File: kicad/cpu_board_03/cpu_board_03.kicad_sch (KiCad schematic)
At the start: 53 parts, among them J1 DIN41612_02x32_AC, J10 PLD_aux, J11 Conn_01x09, J6 Conn_01x02_Socket, J7 Jmp_Irq, J8 Jmp_NMI, J9 Ram1 Enable, SW1 SW_Reset, SW2 SW_PWR, U1 W65C02SxP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

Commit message: routing cpu 3 board
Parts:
- removed J7: Jmp_Irq, Connector_PinHeader_2.54mm:PinHeader_1x02_P2.54mm_Vertical, symbol Connector:Conn_01x02_Pin
- removed J8: Jmp_NMI, Connector_PinHeader_2.54mm:PinHeader_1x02_P2.54mm_Vertical, symbol Connector:Conn_01x02_Pin
- added C1: 47uF, Capacitor_THT:CP_Radial_D4.0mm_P2.00mm, symbol Device:C_Polarized
- added R3, R5: 10K, Resistor_SMD:R_0805_2012Metric_Pad1.20x1.40mm_HandSolder, symbol Device:R
- C3: footprint Package_SO:SO-20_12.8x7.5mm_P1.27mm -> Capacitor_SMD:C_0805_2012Metric_Pad1.18x1.45mm_HandSolder
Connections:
- net AB0: now also J1.a18 (Pin_a18); no longer J1.a17 (Pin_a17)
- net AB1: now also J1.c18 (Pin_c18); no longer J1.a16 (Pin_a16)
- net AB10: now also J1.a13 (Pin_a13); no longer J1.a7 (Pin_a7)
- net AB11: now also J1.c13 (Pin_c13); no longer J1.a6 (Pin_a6)
- net AB12: now also J1.a12 (Pin_a12); no longer J1.a5 (Pin_a5)
- net AB13: now also J1.c12 (Pin_c12); no longer J1.a4 (Pin_a4)
- net AB14: now also J1.a11 (Pin_a11); no longer J1.a3 (Pin_a3)
- net AB15: now also J1.c11 (Pin_c11); no longer J1.a2 (Pin_a2)
- net AB2: now also J1.a17 (Pin_a17); no longer J1.a15 (Pin_a15)
- net AB3: now also J1.c17 (Pin_c17); no longer J1.a14 (Pin_a14)
- net AB4: now also J1.a16 (Pin_a16); no longer J1.a13 (Pin_a13)
- net AB5: now also J1.c16 (Pin_c16); no longer J1.a12 (Pin_a12)
- net AB6: now also J1.a15 (Pin_a15); no longer J1.a11 (Pin_a11)
- net AB7: now also J1.c15 (Pin_c15); no longer J1.a10 (Pin_a10)
- net AB8: now also J1.a14 (Pin_a14); no longer J1.a9 (Pin_a9)
- net AB9: now also J1.c14 (Pin_c14); no longer J1.a8 (Pin_a8)
- net CLOCK: no longer U9.7 (~{ST})
- net DB0: now also J1.a5 (Pin_a5); no longer J1.c9 (Pin_c9)
- net DB1: now also J1.c5 (Pin_c5); no longer J1.c8 (Pin_c8)
- net DB2: now also J1.a4 (Pin_a4); no longer J1.c7 (Pin_c7)
- net DB3: now also J1.c4 (Pin_c4); no longer J1.c6 (Pin_c6)
- net DB4: now also J1.a3 (Pin_a3); no longer J1.c5 (Pin_c5)
- net DB5: now also J1.c3 (Pin_c3); no longer J1.c4 (Pin_c4)
- net DB6: now also J1.a2 (Pin_a2); no longer J1.c3 (Pin_c3)
- net GND: now also J1.c10 (Pin_c10), J1.c27 (Pin_c27), J1.c6 (Pin_c6), C1.2; no longer J1.c18 (Pin_c18)
- net PLD_O0: now also J1.c9 (Pin_c9)
- net PLD_O7: now also J1.c8 (Pin_c8)
- net SYS_CLK: now also J1.a7 (Pin_a7), U9.7 (~{ST}); no longer J1.a22 (Pin_a22)
- net VCC: now also J1.a10 (Pin_a10), J1.a27 (Pin_a27), J1.a6 (Pin_a6), C1.1, R3.1, R5.1; no longer J1.a18 (Pin_a18)
- net ~{IOEN_00_GPIO0}: now also J1.a26 (Pin_a26); no longer J1.a31 (Pin_a31)
- net ~{IOEN_01}: now also J1.c26 (Pin_c26); no longer J1.a30 (Pin_a30)
- net ~{IOEN_02_UART}: now also J1.a25 (Pin_a25)
- net ~{IOEN_03}: now also J1.c25 (Pin_c25); no longer J1.a28 (Pin_a28)
- net ~{IOEN_04}: now also J1.a24 (Pin_a24); no longer J1.a27 (Pin_a27)
- net ~{IOEN_05}: now also J1.c24 (Pin_c24); no longer J1.a26 (Pin_a26)
- net ~{IOEN_06}: now also J1.a23 (Pin_a23); no longer J1.a25 (Pin_a25)
- net ~{IOEN_07}: now also J1.c23 (Pin_c23); no longer J1.a24 (Pin_a24)
- net ~{IO_SEL}: now also J1.a8 (Pin_a8); no longer J1.a23 (Pin_a23)
- net ~{IRQ}: now also J1.a31 (Pin_a31), R5.2
- net ~{NMI}: now also J1.a30 (Pin_a30), R3.2
- net ~{SYS_CLK}: now also J1.c7 (Pin_c7); no longer J1.a21 (Pin_a21)
- net ~{IOEN_02}: no longer names the net of J1.a29 (Pin_a29)
- no-connect marks 30 -> 12

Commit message: more routing on cpu board v3
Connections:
- net ~{CS_RAM0}: now also U4.20 (O3); no longer U4.19 (O4)
- net ~{CS_RAM1}: now also U4.19 (O4); no longer U4.20 (O3)
- net at D8.1 (K): now also RN2.2 (R2.1); no longer RN2.4 (R4.1)
- net at D3.1 (K): now also RN1.1 (R1.1); no longer RN1.3 (R3.1)
- net at D9.2 (A): now also RN3.2 (R2.1); no longer RN3.4 (R4.1)
- net at D6.1 (K): now also RN2.4 (R4.1); no longer RN2.2 (R2.1)
- net at D11.2 (A): now also RN3.3 (R3.1); no longer RN3.2 (R2.1)
- net at D10.2 (A): now also RN3.4 (R4.1); no longer RN3.3 (R3.1)
- net at D1.1 (K): now also RN1.3 (R3.1); no longer RN1.1 (R1.1)
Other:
- moved on the sheet: RN1, RN2

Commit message: more routing
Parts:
- added C13, C15, C2: 100nF, Capacitor_SMD:C_0805_2012Metric_Pad1.18x1.45mm_HandSolder, symbol Device:C
- added U12: 74LS138, Package_SO:SO-16_3.9x9.9mm_P1.27mm, symbol 74xx:74LS138
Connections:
- net A4: now also U12.1 (A0)
- net A5: now also U12.2 (A1)
- net A6: now also U12.3 (A2)
- net A7: now also U12.6 (E3)
- net GND: now also J1.c19 (Pin_c19), J1.c29 (Pin_c29), J10.1 (Pin_1), J9.1 (Pin_1), U8.19 (CE), C13.2, C15.2, C2.2, U12.5 (E2), U12.8 (GND); no longer J1.c27 (Pin_c27), J9.3 (Pin_3), U10.1 (A->B), U11.1 (A->B)
- net PLD_I1: now also J10.2 (Pin_2); no longer J10.1 (Pin_1)
- net PLD_O0: no longer J10.2 (Pin_2)
- net RES: now also J1.c31 (Pin_c31); no longer J1.c30 (Pin_c30)
- net VCC: now also J1.a19 (Pin_a19), J1.a29 (Pin_a29), J10.3 (Pin_3), J9.3 (Pin_3), U10.1 (A->B), U11.1 (A->B), C13.1, C15.1, C2.1, U12.16 (VCC); no longer J1.a27 (Pin_a27), J9.1 (Pin_1)
- net ~{IOEN_00_GPIO0}: now also J1.a24 (Pin_a24); no longer J1.a26 (Pin_a26)
- net ~{IOEN_01}: now also J1.c24 (Pin_c24); no longer J1.c26 (Pin_c26)
- net ~{IOEN_02_UART}: now also J1.a23 (Pin_a23); no longer J1.a25 (Pin_a25)
- net ~{IOEN_03}: now also J1.c23 (Pin_c23); no longer J1.c25 (Pin_c25)
- net ~{IOEN_04}: now also J1.a22 (Pin_a22); no longer J1.a24 (Pin_a24)
- net ~{IOEN_05}: now also J1.c22 (Pin_c22); no longer J1.c24 (Pin_c24)
- net ~{IOEN_06}: now also J1.a21 (Pin_a21); no longer J1.a23 (Pin_a23)
- net ~{IOEN_07}: now also J1.c21 (Pin_c21); no longer J1.c23 (Pin_c23)
- net ~{IO_SEL}: now also U12.4 (E1)
- net ~{IRQ}: now also J1.a30 (Pin_a30); no longer J1.a31 (Pin_a31)
- net ~{NMI}: now also J1.c30 (Pin_c30); no longer J1.a30 (Pin_a30)
- net ~{RES}: now also J1.a31 (Pin_a31); no longer J1.c31 (Pin_c31)
- net ~{IO_RD_DIR}: now reaches U8.1 (A->B)
- net ~{IO_RD_DIR}: now also J1.c8 (Pin_c8), U4.16 (O7)
- net ~{IOEN_08}: now reaches J1.a28 (Pin_a28)
- net ~{IOEN_08}: now also U12.15 (O0)
- net ~{IOEN_09}: now reaches J1.c28 (Pin_c28)
- net ~{IOEN_09}: now also U12.14 (O1)
- removed net PLD_O7: J1.c8 (Pin_c8), J10.3 (Pin_3), U4.16 (O7)
- new net ~{IOEN_10}: J1.a27 (Pin_a27), U12.13 (O2)
- new net ~{IOEN_11}: J1.c27 (Pin_c27), U12.12 (O3)
- new net ~{IOEN_12}: J1.a26 (Pin_a26), U12.11 (O4)
- new net ~{IOEN_13}: J1.c26 (Pin_c26), U12.10 (O5)
- new net ~{IOEN_14}: J1.a25 (Pin_a25), U12.9 (O6)
- new net ~{IOEN_15}: J1.c25 (Pin_c25), U12.7 (O7)
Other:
- moved on the sheet: C1, C11, C12, D1, D11, D12, J10, J11, RN1, RN2, RN3, U6

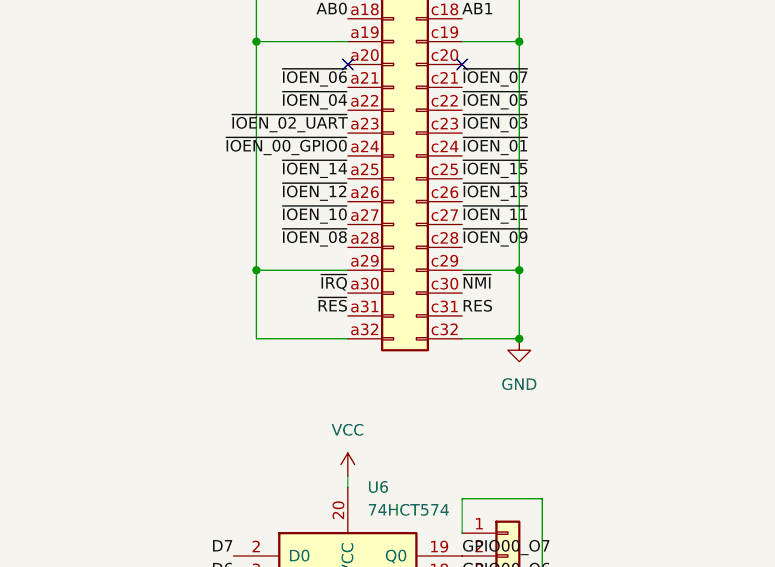
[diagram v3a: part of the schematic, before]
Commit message: shrink board
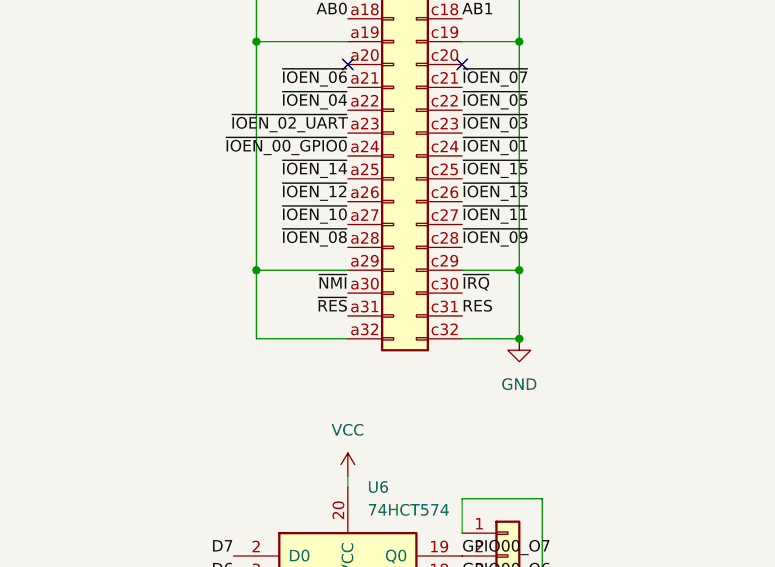
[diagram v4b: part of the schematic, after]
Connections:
- net ~{IRQ}: now also J1.c30 (Pin_c30); no longer J1.a30 (Pin_a30)
- net ~{NMI}: now also J1.a30 (Pin_a30); no longer J1.c30 (Pin_c30)
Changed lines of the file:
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@@
+    (effects (font (size 1.27 1.27)) (justify right bottom))
+  )
+  (label "~{NMI}" (at 351.79 185.42 180) (fields_autoplaced)
     (effects (font (size 1.27 1.27)) (justify right bottom))
   )
@@
     (effects (font (size 1.27 1.27)) (justify left bottom))
   )
-  (label "~{IRQ}" (at 351.79 185.42 180) (fields_autoplaced)
-    (effects (font (size 1.27 1.27)) (justify right bottom))
-  )
   (label "A3" (at 261.62 175.26 0) (fields_autoplaced)
     (effects (font (size 1.27 1.27)) (justify left bottom))
@@
     (effects (font (size 1.27 1.27)) (justify right bottom))
   )
-  (label "~{NMI}" (at 364.49 185.42 0) (fields_autoplaced)
-    (effects (font (size 1.27 1.27)) (justify left bottom))
-  )
   (label "A1" (at 82.55 135.89 180) (fields_autoplaced)
     (effects (font (size 1.27 1.27)) (justify right bottom))
@@
     (effects (font (size 1.27 1.27)) (justify right bottom))
   )
+  (label "~{IRQ}" (at 364.49 185.42 0) (fields_autoplaced)
+    (effects (font (size 1.27 1.27)) (justify left bottom))
+  )
   (label "D0" (at 339.09 232.41 180) (fields_autoplaced)

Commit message: DRCs pass...
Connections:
- net ~{IOEN_00_GPIO0}: now also J1.a28 (Pin_a28); no longer J1.a24 (Pin_a24)
- net ~{IOEN_01}: now also J1.c28 (Pin_c28); no longer J1.c24 (Pin_c24)
- net ~{IOEN_02_UART}: now also J1.a27 (Pin_a27); no longer J1.a23 (Pin_a23)
- net ~{IOEN_03}: now also J1.c27 (Pin_c27); no longer J1.c23 (Pin_c23)
- net ~{IOEN_04}: now also J1.a26 (Pin_a26); no longer J1.a22 (Pin_a22)
- net ~{IOEN_05}: now also J1.c26 (Pin_c26); no longer J1.c22 (Pin_c22)
- net ~{IOEN_06}: now also J1.a25 (Pin_a25); no longer J1.a21 (Pin_a21)
- net ~{IOEN_07}: now also J1.c25 (Pin_c25); no longer J1.c21 (Pin_c21)
- net ~{IOEN_08}: now also J1.a24 (Pin_a24); no longer J1.a28 (Pin_a28)
- net ~{IOEN_09}: now also J1.c24 (Pin_c24); no longer J1.c28 (Pin_c28)
- net ~{IOEN_10}: now also J1.a23 (Pin_a23); no longer J1.a27 (Pin_a27)
- net ~{IOEN_11}: now also J1.c23 (Pin_c23); no longer J1.c27 (Pin_c27)
- net ~{IOEN_12}: now also J1.a22 (Pin_a22); no longer J1.a26 (Pin_a26)
- net ~{IOEN_13}: now also J1.c22 (Pin_c22); no longer J1.c26 (Pin_c26)
- net ~{IOEN_14}: now also J1.a21 (Pin_a21); no longer J1.a25 (Pin_a25)
- net ~{IOEN_15}: now also J1.c21 (Pin_c21); no longer J1.c25 (Pin_c25)
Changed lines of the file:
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@@
+    (effects (font (size 1.27 1.27)) (justify left bottom))
+  )
+  (label "~{IOEN_10}" (at 351.79 167.64 180) (fields_autoplaced)
+    (effects (font (size 1.27 1.27)) (justify right bottom))
+  )
+  (label "~{IOEN_13}" (at 364.49 165.1 0) (fields_autoplaced)
     (effects (font (size 1.27 1.27)) (justify left bottom))
   )
@@
     (effects (font (size 1.27 1.27)) (justify left bottom))
   )
-  (label "~{IOEN_15}" (at 364.49 172.72 0) (fields_autoplaced)
-    (effects (font (size 1.27 1.27)) (justify left bottom))
+  (label "~{IOEN_14}" (at 351.79 162.56 180) (fields_autoplaced)
+    (effects (font (size 1.27 1.27)) (justify right bottom))
   )
   (label "~{IOEN_12}" (at 175.26 255.27 0) (fields_autoplaced)
@@
     (effects (font (size 1.27 1.27)) (justify right bottom))
   )
+  (label "~{IOEN_06}" (at 351.79 172.72 180) (fields_autoplaced)
+    (effects (font (size 1.27 1.27)) (justify right bottom))
+  )
   (label "DB6" (at 285.75 129.54 0) (fields_autoplaced)
     (effects (font (size 1.27 1.27)) (justify left bottom))
@@
     (effects (font (size 1.27 1.27)) (justify left bottom))
   )
+  (label "~{IOEN_04}" (at 351.79 175.26 180) (fields_autoplaced)
+    (effects (font (size 1.27 1.27)) (justify right bottom))
+  )
   (label "A10" (at 35.56 246.38 180) (fields_autoplaced)
     (effects (font (size 1.27 1.27)) (justify right bottom))
@@
     (effects (font (size 1.27 1.27)) (justify right bottom))
   )
-  (label "~{IOEN_13}" (at 364.49 175.26 0) (fields_autoplaced)
-    (effects (font (size 1.27 1.27)) (justify left bottom))
-  )
   (label "GPIO00_O7" (at 364.49 214.63 0) (fields_autoplaced)
     (effects (font (size 1.27 1.27)) (justify left bottom))
@@
     (effects (font (size 1.27 1.27)) (justify left bottom))
   )
+  (label "~{IOEN_08}" (at 351.79 170.18 180) (fields_autoplaced)
+    (effects (font (size 1.27 1.27)) (justify right bottom))
+  )
   (label "~{IO_RD_DIR}" (at 259.08 137.16 180) (fields_autoplaced)
     (effects (font (size 1.27 1.27)) (justify right bottom))
@@
     (effects (font (size 1.27 1.27)) (justify left bottom))
   )
-  (label "~{IOEN_09}" (at 364.49 180.34 0) (fields_autoplaced)
-    (effects (font (size 1.27 1.27)) (justify left bottom))
-  )
   (label "A0" (at 134.62 135.89 180) (fields_autoplaced)
     (effects (font (size 1.27 1.27)) (justify right bottom))
@@
     (effects (font (size 1.27 1.27)) (justify right bottom))
   )
+  (label "~{IOEN_01}" (at 364.49 180.34 0) (fields_autoplaced)
+    (effects (font (size 1.27 1.27)) (justify left bottom))
+  )
   (label "A1" (at 58.42 119.38 0) (fields_autoplaced)
     (effects (font (size 1.27 1.27)) (justify left bottom))
@@
     (effects (font (size 1.27 1.27)) (justify left bottom))
   )
+  (label "~{IOEN_03}" (at 364.49 177.8 0) (fields_autoplaced)
+    (effects (font (size 1.27 1.27)) (justify left bottom))
+  )
   (label "A3" (at 134.62 143.51 180) (fields_autoplaced)
     (effects (font (size 1.27 1.27)) (justify right bottom))
@@
     (effects (font (size 1.27 1.27)) (justify left bottom))
   )
-  (label "~{IOEN_14}" (at 351.79 172.72 180) (fields_autoplaced)
-    (effects (font (size 1.27 1.27)) (justify right bottom))
-  )
   (label "SYS_CLK" (at 35.56 121.92 180) (fields_autoplaced)
     (effects (font (size 1.27 1.27)) (justify right bottom))
@@
     (effects (font (size 1.27 1.27)) (justify left bottom))
   )
+  (label "~{IOEN_11}" (at 364.49 167.64 0) (fields_autoplaced)
+    (effects (font (size 1.27 1.27)) (justify left bottom))
+  )
   (label "A3" (at 58.42 124.46 0) (fields_autoplaced)
     (effects (font (size 1.27 1.27)) (justify left bottom))
@@
     (effects (font (size 1.27 1.27)) (justify right bottom))
   )
+  (label "~{IOEN_07}" (at 364.49 172.72 0) (fields_autoplaced)
+    (effects (font (size 1.27 1.27)) (justify left bottom))
+  )
   (label "~{IOEN_02_UART}" (at 116.84 248.92 0) (fields_autoplaced)
     (effects (font (size 1.27 1.27)) (justify left bottom))
@@
     (effects (font (size 1.27 1.27)) (justify left bottom))
   )
-  (label "~{IOEN_07}" (at 364.49 162.56 0) (fields_autoplaced)
-    (effects (font (size 1.27 1.27)) (justify left bottom))
-  )
   (label "AB3" (at 364.49 152.4 0) (fields_autoplaced)
     (effects (font (size 1.27 1.27)) (justify left bottom))
@@
     (effects (font (size 1.27 1.27)) (justify left bottom))
   )
-  (label "~{IOEN_06}" (at 351.79 162.56 180) (fields_autoplaced)
-    (effects (font (size 1.27 1.27)) (justify right bottom))
-  )
-  (label "~{IOEN_05}" (at 364.49 165.1 0) (fields_autoplaced)
-    (effects (font (size 1.27 1.27)) (justify left bottom))
-  )
   (label "A3" (at 261.62 175.26 0) (fields_autoplaced)
     (effects (font (size 1.27 1.27)) (justify left bottom))
@@
     (effects (font (size 1.27 1.27)) (justify right bottom))
   )
+  (label "~{IOEN_15}" (at 364.49 162.56 0) (fields_autoplaced)
+    (effects (font (size 1.27 1.27)) (justify left bottom))
+  )
   (label "DB1" (at 285.75 116.84 0) (fields_autoplaced)
     (effects (font (size 1.27 1.27)) (justify left bottom))
@@
     (effects (font (size 1.27 1.27)) (justify right bottom))
   )
+  (label "~{IOEN_05}" (at 364.49 175.26 0) (fields_autoplaced)
+    (effects (font (size 1.27 1.27)) (justify left bottom))
+  )
   (label "A13" (at 58.42 149.86 0) (fields_autoplaced)
     (effects (font (size 1.27 1.27)) (justify left bottom))
@@
     (effects (font (size 1.27 1.27)) (justify right bottom))
   )
+  (label "~{IOEN_02_UART}" (at 351.79 177.8 180) (fields_autoplaced)
+    (effects (font (size 1.27 1.27)) (justify right bottom))
+  )
   (label "A0" (at 58.42 116.84 0) (fields_autoplaced)
     (effects (font (size 1.27 1.27)) (justify left bottom))
@@
     (effects (font (size 1.27 1.27)) (justify left bottom))
   )
-  (label "~{IOEN_04}" (at 351.79 165.1 180) (fields_autoplaced)
-    (effects (font (size 1.27 1.27)) (justify right bottom))
-  )
   (label "AB13" (at 364.49 139.7 0) (fields_autoplaced)
     (effects (font (size 1.27 1.27)) (justify left bottom))
@@
     (effects (font (size 1.27 1.27)) (justify right bottom))
   )
-  (label "~{IOEN_12}" (at 351.79 175.26 180) (fields_autoplaced)
-    (effects (font (size 1.27 1.27)) (justify right bottom))
-  )
   (label "~{IOEN_05}" (at 116.84 256.54 0) (fields_autoplaced)
     (effects (font (size 1.27 1.27)) (justify left bottom))
@@
     (effects (font (size 1.27 1.27)) (justify left bottom))
   )
+  (label "~{IOEN_00_GPIO0}" (at 351.79 180.34 180) (fields_autoplaced)
+    (effects (font (size 1.27 1.27)) (justify right bottom))
+  )
   (label "A4" (at 180.34 139.7 180) (fields_autoplaced)
     (effects (font (size 1.27 1.27)) (justify right bottom))
@@
     (effects (font (size 1.27 1.27)) (justify right bottom))
   )
-  (label "~{IOEN_02_UART}" (at 351.79 167.64 180) (fields_autoplaced)
-    (effects (font (size 1.27 1.27)) (justify right bottom))
-  )
   (label "AB9" (at 364.49 144.78 0) (fields_autoplaced)
     (effects (font (size 1.27 1.27)) (justify left bottom))
   )
+  (label "~{IOEN_12}" (at 351.79 165.1 180) (fields_autoplaced)
+    (effects (font (size 1.27 1.27)) (justify right bottom))
+  )
   (label "D3" (at 162.56 143.51 0) (fields_autoplaced)
     (effects (font (size 1.27 1.27)) (justify left bottom))
@@
     (effects (font (size 1.27 1.27)) (justify right bottom))
   )
-  (label "~{IOEN_10}" (at 351.79 177.8 180) (fields_autoplaced)
-    (effects (font (size 1.27 1.27)) (justify right bottom))
-  )
   (label "A12" (at 82.55 163.83 180) (fields_autoplaced)
     (effects (font (size 1.27 1.27)) (justify right bottom))
@@
     (effects (font (size 1.27 1.27)) (justify left bottom))
   )
-  (label "~{IOEN_03}" (at 364.49 167.64 0) (fields_autoplaced)
-    (effects (font (size 1.27 1.27)) (justify left bottom))
-  )
-  (label "~{IOEN_00_GPIO0}" (at 351.79 170.18 180) (fields_autoplaced)
-    (effects (font (size 1.27 1.27)) (justify right bottom))
-  )
   (label "D2" (at 58.42 165.1 0) (fields_autoplaced)
     (effects (font (size 1.27 1.27)) (justify left bottom))
@@
     (effects (font (size 1.27 1.27)) (justify left bottom))
   )
-  (label "~{IOEN_11}" (at 364.49 177.8 0) (fields_autoplaced)
-    (effects (font (size 1.27 1.27)) (justify left bottom))
-  )
   (label "~{QOE}" (at 180.34 175.26 180) (fields_autoplaced)
     (effects (font (size 1.27 1.27)) (justify right bottom))
@@
     (effects (font (size 1.27 1.27)) (justify left bottom))
   )
-  (label "~{IOEN_08}" (at 351.79 180.34 180) (fields_autoplaced)
-    (effects (font (size 1.27 1.27)) (justify right bottom))
-  )
   (label "~{CS_ROM}" (at 180.34 172.72 180) (fields_autoplaced)
     (effects (font (size 1.27 1.27)) (justify right bottom))
@@
     (effects (font (size 1.27 1.27)) (justify right bottom))
   )
-  (label "~{IOEN_01}" (at 364.49 170.18 0) (fields_autoplaced)
-    (effects (font (size 1.27 1.27)) (justify left bottom))
-  )
   (label "A5" (at 261.62 180.34 0) (fields_autoplaced)
     (effects (font (size 1.27 1.27)) (justify left bottom))
@@
     (effects (font (size 1.27 1.27)) (justify left bottom))
   )
+  (label "~{IOEN_09}" (at 364.49 170.18 0) (fields_autoplaced)
+    (effects (font (size 1.27 1.27)) (justify left bottom))
+  )

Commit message: use socket footprint for xtal
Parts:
- X1: footprint Package_DIP:DIP-14_W7.62mm -> Package_DIP:DIP-14_W7.62mm_Socket
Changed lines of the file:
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@@
       (effects (font (size 1.27 1.27)) (justify right))
     )
-    (property "Footprint" "Package_DIP:DIP-14_W7.62mm" (at 96.52 38.1 0)
+    (property "Footprint" "Package_DIP:DIP-14_W7.62mm_Socket" (at 96.52 38.1 0)
       (effects (font (size 1.27 1.27)) hide)
     )

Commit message: routing improvements
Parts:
- J10: footprint Connector_PinSocket_2.54mm:PinSocket_1x03_P2.54mm_Vertical -> Connector_PinHeader_2.54mm:PinHeader_1x03_P2.54mm_Vertical
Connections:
- net GND: now also U10.1 (A->B), U11.1 (A->B)
- net VCC: no longer U10.1 (A->B), U11.1 (A->B)
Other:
- moved on the sheet: C1, C10, C11, C12, C13, C14, C15, C2, C3, C4, C5, C6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
